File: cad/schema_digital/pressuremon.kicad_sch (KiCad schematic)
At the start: 10 parts, among them J1 Conn_01x04_Pin, J2 Conn_01x04_Pin, J3 Conn_01x03_Pin, U3 DS18B20

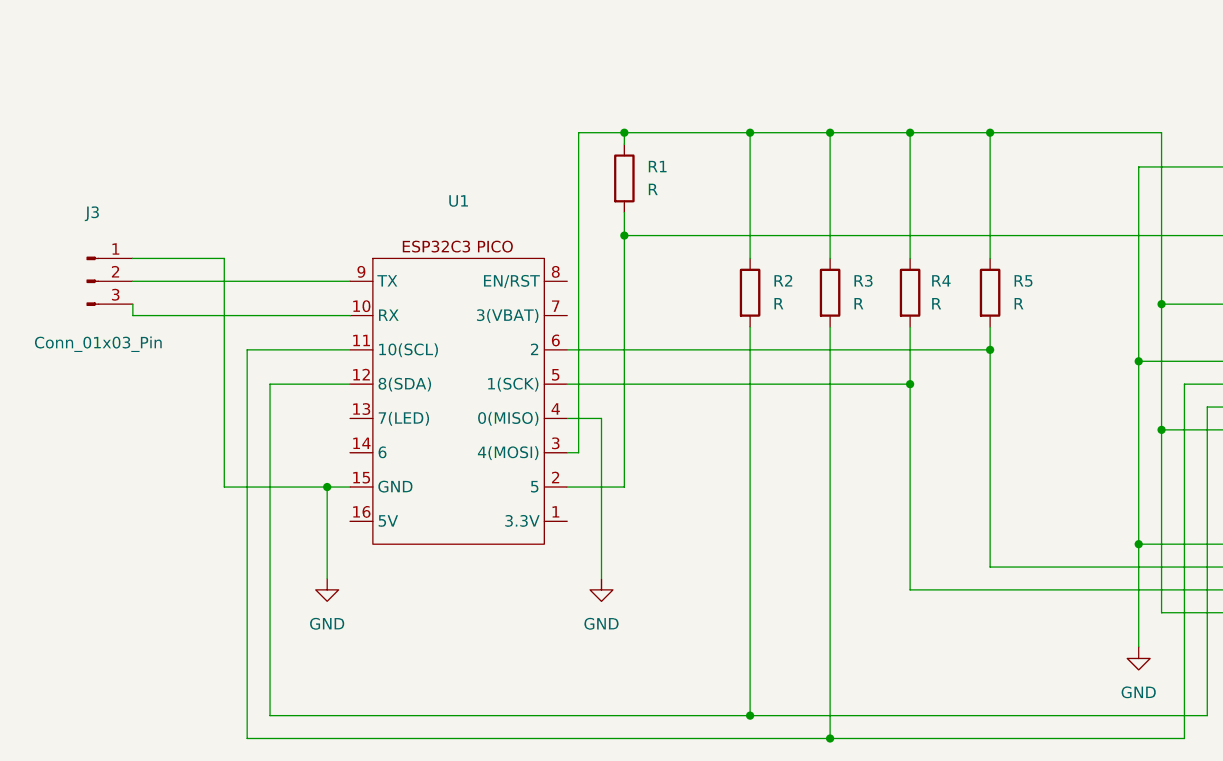
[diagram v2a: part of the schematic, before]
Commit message: Updating schematic, adding off switch
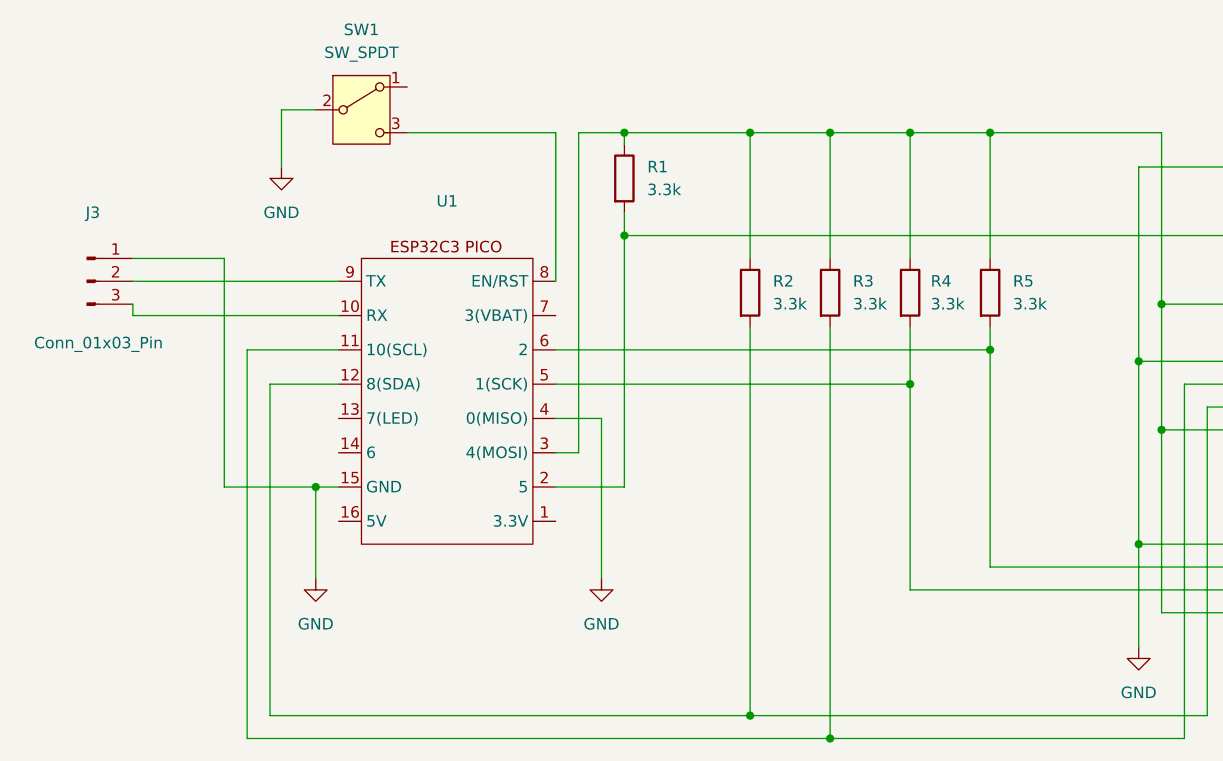
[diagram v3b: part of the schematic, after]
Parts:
- added SW1: SW_SPDT, Connector_PinHeader_2.54mm:PinHeader_1x03_P2.54mm_Vertical, symbol Switch:SW_SPDT
- R1, R2, R3, R4, R5: value R -> 3.3k
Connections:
- net GND: now also SW1.2 (B)
- net at U1.8 (EN/RST): now also SW1.3 (C)
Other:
- moved on the sheet: U1
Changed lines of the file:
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@@
-	)
-	(junction
-		(at 50.8 88.9)
-		(diameter 0)
-		(color 0 0 0 0)
 	)
 	(junction
@@
 		(color 0 0 0 0)
 	)
+	(junction
+		(at 49.53 88.9)
+		(diameter 0)
+		(color 0 0 0 0)
+	)
 	(wire
 		(pts
@@
 	(wire
 		(pts
+			(xy 76.2 49.53) (xy 76.2 66.04)
+		)
+		(stroke
+			(width 0)
+			(type default)
+		)
+	)
+	(wire
+		(pts
 			(xy 115.57 100.33) (xy 160.02 100.33)
 		)
@@
 	(wire
 		(pts
-			(xy 39.37 88.9) (xy 50.8 88.9)
+			(xy 39.37 88.9) (xy 49.53 88.9)
 		)
 		(stroke
@@
 	(wire
 		(pts
-			(xy 53.34 88.9) (xy 50.8 88.9)
-		)
-		(stroke
-			(width 0)
-			(type default)
-		)
-	)
-	(wire
-		(pts
 			(xy 160.02 74.93) (xy 140.97 74.93)
 		)
@@
 	(wire
 		(pts
+			(xy 49.53 88.9) (xy 52.07 88.9)
+		)
+		(stroke
+			(width 0)
+			(type default)
+		)
+	)
+	(wire
+		(pts
 			(xy 83.82 60.96) (xy 160.02 60.96)
 		)
@@
 	(wire
 		(pts
-			(xy 29.21 69.85) (xy 53.34 69.85)
-		)
-		(stroke
-			(width 0)
-			(type default)
-		)
-	)
-	(wire
-		(pts
-			(xy 78.74 85.09) (xy 77.47 85.09)
+			(xy 45.72 46.99) (xy 49.53 46.99)
+		)
+		(stroke
+			(width 0)
+			(type default)
+		)
+	)
+	(wire
+		(pts
+			(xy 29.21 69.85) (xy 52.07 69.85)
+		)
+		(stroke
+			(width 0)
+			(type default)
+		)
+	)
+	(wire
+		(pts
+			(xy 78.74 85.09) (xy 76.2 85.09)
 		)
 		(stroke
@@
 	(wire
 		(pts
+			(xy 45.72 53.34) (xy 45.72 46.99)
+		)
+		(stroke
+			(width 0)
+			(type default)
+		)
+	)
+	(wire
+		(pts
 			(xy 148.59 80.01) (xy 160.02 80.01)
 		)
@@
 	(wire
 		(pts
-			(xy 44.45 77.47) (xy 53.34 77.47)
+			(xy 44.45 77.47) (xy 52.07 77.47)
 		)
 		(stroke
@@
 	(wire
 		(pts
-			(xy 83.82 88.9) (xy 77.47 88.9)
+			(xy 83.82 88.9) (xy 76.2 88.9)
 		)
 		(stroke
@@
 	(wire
 		(pts
-			(xy 77.47 73.66) (xy 124.46 73.66)
+			(xy 76.2 73.66) (xy 124.46 73.66)
 		)
 		(stroke
@@
 	(wire
 		(pts
-			(xy 29.21 66.04) (xy 53.34 66.04)
+			(xy 29.21 66.04) (xy 52.07 66.04)
 		)
 		(stroke
@@
 	(wire
 		(pts
-			(xy 77.47 77.47) (xy 115.57 77.47)
+			(xy 76.2 77.47) (xy 115.57 77.47)
 		)
 		(stroke
@@
 	(wire
 		(pts
-			(xy 50.8 88.9) (xy 50.8 99.06)
+			(xy 49.53 88.9) (xy 49.53 99.06)
 		)
 		(stroke
@@
 	(wire
 		(pts
-			(xy 77.47 81.28) (xy 81.28 81.28)
+			(xy 76.2 81.28) (xy 81.28 81.28)
 		)
 		(stroke
@@
 	(wire
 		(pts
+			(xy 59.69 49.53) (xy 76.2 49.53)
+		)
+		(stroke
+			(width 0)
+			(type default)
+		)
+	)
+	(wire
+		(pts
 			(xy 29.21 69.85) (xy 29.21 68.58)
 		)
@@
 	(wire
 		(pts
-			(xy 41.91 73.66) (xy 53.34 73.66)
+			(xy 41.91 73.66) (xy 52.07 73.66)
 		)
 		(stroke
@@
 	)
 	(symbol
+		(lib_id "Switch:SW_SPDT")
+		(at 54.61 46.99 0)
+		(unit 1)
+		(exclude_from_sim no)
+		(in_bom yes)
+		(on_board yes)
+		(dnp no)
+		(fields_autoplaced yes)
+		(property "Reference" "SW1"
+			(at 54.61 38.1 0)
+			(effects
+				(font
+					(size 1.27 1.27)
+				)
+			)
+		)
+		(property "Value" "SW_SPDT"
+			(at 54.61 40.64 0)
+			(effects
+				(font
+					(size 1.27 1.27)
+				)
+			)
+		)
+		(property "Footprint" "Connector_PinHeader_2.54mm:PinHeader_1x03_P2.54mm_Vertical"
+			(at 54.61 46.99 0)
+			(effects
+				(font
+					(size 1.27 1.27)
+				)
+				(hide yes)
+			)
+		)
+		(property "Datasheet" "~"
+			(at 54.61 54.61 0)
+			(effects
+				(font
+					(size 1.27 1.27)
+				)
+				(hide yes)
+			)
+		)
+		(property "Description" "Switch, single pole double throw"
+			(at 54.61 46.99 0)
+			(effects
+				(font
+					(size 1.27 1.27)
+				)
+				(hide yes)
+			)
+		)
+		(pin "1"
+		)
+		(pin "3"
+		)
+		(pin "2"
+		)
+		(instances
+			(project ""
+				(path "/42dbddbd-b9bd-46e0-88a7-2826e12ac31d"
+					(reference "SW1")
+					(unit 1)
+				)
+			)
+		)
+	)
+	(symbol
 		(lib_id "Device:R")
 		(at 124.46 67.31 0)
@@
 			)
 		)
-		(property "Value" "R"
+		(property "Value" "3.3k"
 			(at 127 68.5799 0)
 			(effects
@@
 			)
 		)
-		(property "Value" "R"
+		(property "Value" "3.3k"
 			(at 100.33 68.5799 0)
 			(effects
@@
 				(path "/42dbddbd-b9bd-46e0-88a7-2826e12ac31d"
 					(reference "R2")
+					(unit 1)
+				)
+			)
+		)
+	)
+	(symbol
+		(lib_id "power:GND")
+		(at 45.72 53.34 0)
+		(unit 1)
+		(exclude_from_sim no)
+		(in_bom yes)
+		(on_board yes)
+		(dnp no)
+		(fields_autoplaced yes)
+		(property "Reference" "#PWR03"
+			(at 45.72 59.69 0)
+			(effects
+				(font
+					(size 1.27 1.27)
+				)
+				(hide yes)
+			)
+		)
+		(property "Value" "GND"
+			(at 45.72 58.42 0)
+			(effects
+				(font
+					(size 1.27 1.27)
+				)
+			)
+		)
+		(property "Footprint" ""
+			(at 45.72 53.34 0)
+			(effects
+				(font
+					(size 1.27 1.27)
+				)
+				(hide yes)
+			)
+		)
+		(property "Datasheet" ""
+			(at 45.72 53.34 0)
+			(effects
+				(font
+					(size 1.27 1.27)
+				)
+				(hide yes)
+			)
+		)
+		(property "Description" "Power symbol creates a global label with name \"GND\" , ground"
+			(at 45.72 53.34 0)
+			(effects
+				(font
+					(size 1.27 1.27)
+				)
+				(hide yes)
+			)
+		)
+		(pin "1"
+		)
+		(instances
+			(project "pressuremon"
+				(path "/42dbddbd-b9bd-46e0-88a7-2826e12ac31d"
+					(reference "#PWR03")
 					(unit 1)
 				)
@@
 			)
 		)
-		(property "Value" "R"
+		(property "Value" "3.3k"
 			(at 109.22 68.5799 0)
 			(effects
@@
 	(symbol
 		(lib_id "pressuremon_library:ESP32C3-pico")
-		(at 59.69 80.01 0)
+		(at 58.42 80.01 0)
 		(unit 1)
 		(exclude_from_sim no)
@@
 		(fields_autoplaced yes)
 		(property "Reference" "U1"
-			(at 65.405 57.15 0)
+			(at 64.135 57.15 0)
 			(effects
 				(font
@@
 		)
 		(property "Value" "~"
-			(at 65.405 59.69 0)
+			(at 64.135 59.69 0)
 			(effects
 				(font
@@
 		)
 		(property "Footprint" "pressuremon_library:ESP32C3-pico"
-			(at 59.69 80.01 0)
+			(at 58.42 80.01 0)
 			(effects
 				(font
@@
 		)
 		(property "Datasheet" ""
-			(at 59.69 80.01 0)
+			(at 58.42 80.01 0)
 			(effects
 				(font
@@
 		)
 		(property "Description" ""
-			(at 59.69 80.01 0)
+			(at 58.42 80.01 0)
 			(effects
 				(font
@@
 			)
 		)
-		(property "Value" "R"
+		(property "Value" "3.3k"
 			(at 117.856 68.58 0)
 			(effects
@@
 			)
 		)
-		(property "Value" "R"
+		(property "Value" "3.3k"
 			(at 86.36 55.8799 0)
 			(effects
@@
 	(symbol
 		(lib_id "power:GND")
-		(at 50.8 99.06 0)
+		(at 49.53 99.06 0)
 		(unit 1)
 		(exclude_from_sim no)
@@
 		(fields_autoplaced yes)
 		(property "Reference" "#PWR2"
-			(at 50.8 105.41 0)
+			(at 49.53 105.41 0)
 			(effects
 				(font
@@
 		)
 		(property "Value" "GND"
-			(at 50.8 104.14 0)
+			(at 49.53 104.14 0)
 			(effects
 				(font
@@
 		)
 		(property "Footprint" ""
-			(at 50.8 99.06 0)
+			(at 49.53 99.06 0)
 			(effects
 				(font
@@
 		)
 		(property "Datasheet" ""
-			(at 50.8 99.06 0)
+			(at 49.53 99.06 0)
 			(effects
 				(font
@@
 		)
 		(property "Description" "Power symbol creates a global label with name \"GND\" , ground"
-			(at 50.8 99.06 0)
-			(effects
-				(font
+			(at 49.53 99.06 0)
+			(effects
+				(font

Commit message: Update pcb to v1.3
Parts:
- U3: footprint Package_TO_SOT_THT:TO-92_Inline -> Package_TO_SOT_THT:TO-92L_Inline_Wide
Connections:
- net GND: now also SW1.1 (A)
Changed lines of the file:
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@@
+	)
+	(junction
+		(at 45.72 46.99)
+		(diameter 0)
+		(color 0 0 0 0)
 	)
 	(junction
@@
 	(wire
 		(pts
+			(xy 45.72 31.75) (xy 45.72 46.99)
+		)
+		(stroke
+			(width 0)
+			(type default)
+		)
+	)
+	(wire
+		(pts
 			(xy 97.79 49.53) (xy 106.68 49.53)
 		)
@@
 	(wire
 		(pts
+			(xy 63.5 31.75) (xy 45.72 31.75)
+		)
+		(stroke
+			(width 0)
+			(type default)
+		)
+	)
+	(wire
+		(pts
 			(xy 106.68 49.53) (xy 106.68 63.5)
 		)
@@
 	(wire
 		(pts
+			(xy 63.5 44.45) (xy 63.5 31.75)
+		)
+		(stroke
+			(width 0)
+			(type default)
+		)
+	)
+	(wire
+		(pts
 			(xy 78.74 85.09) (xy 78.74 49.53)
 		)
@@
 		(pts
 			(xy 106.68 71.12) (xy 106.68 116.84)
+		)
+		(stroke
+			(width 0)
+			(type default)
+		)
+	)
+	(wire
+		(pts
+			(xy 59.69 44.45) (xy 63.5 44.45)
 		)
 		(stroke
@@
 			)
 		)
-		(property "Footprint" "Package_TO_SOT_THT:TO-92_Inline"
+		(property "Footprint" "Package_TO_SOT_THT:TO-92L_Inline_Wide"
 			(at 193.04 54.61 0)
 			(effects

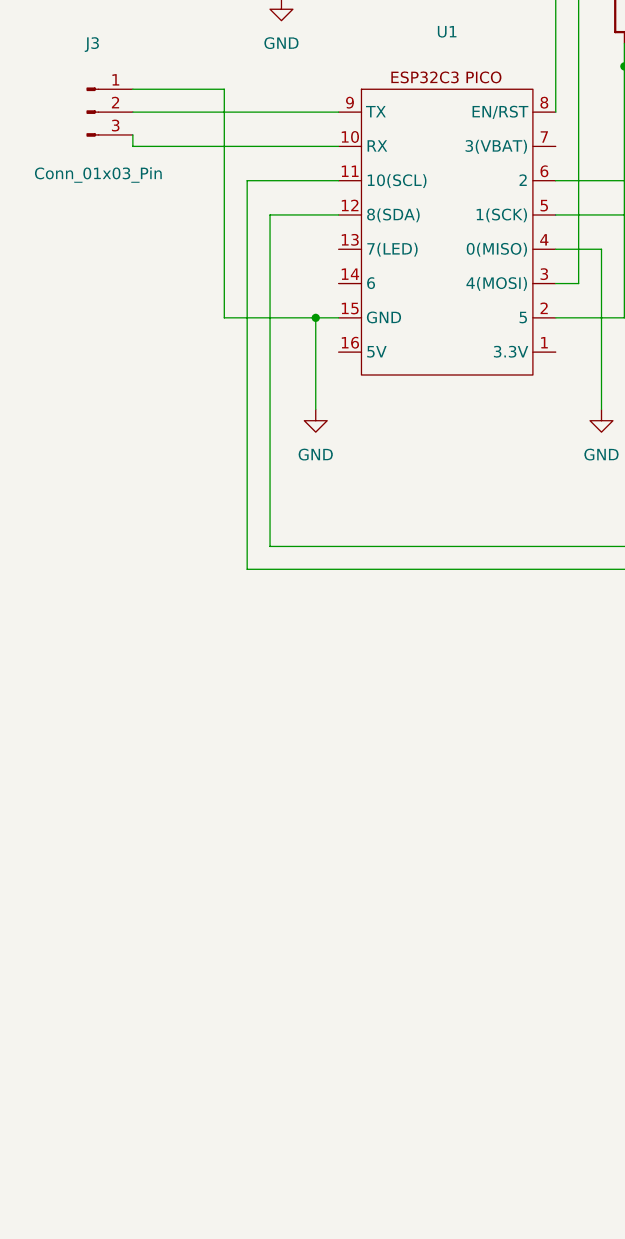
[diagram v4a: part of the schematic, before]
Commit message: Adding mounting holes to pcb
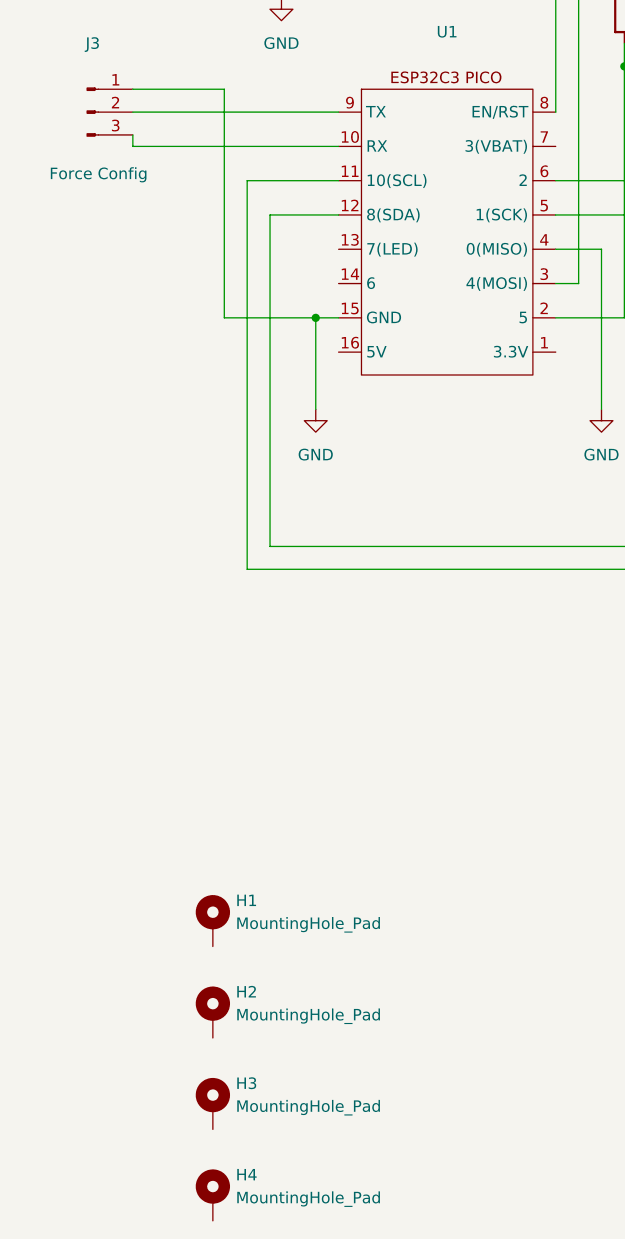
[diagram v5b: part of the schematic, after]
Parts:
- added H1, H2, H3, H4: MountingHole_Pad, MountingHole:MountingHole_2.2mm_M2_ISO7380_Pad, symbol Mechanical:MountingHole_Pad
- J3: value Conn_01x03_Pin -> Force Config
